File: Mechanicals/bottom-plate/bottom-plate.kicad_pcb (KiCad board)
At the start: 2 copper layers, 89 x 100 mm, 4 parts

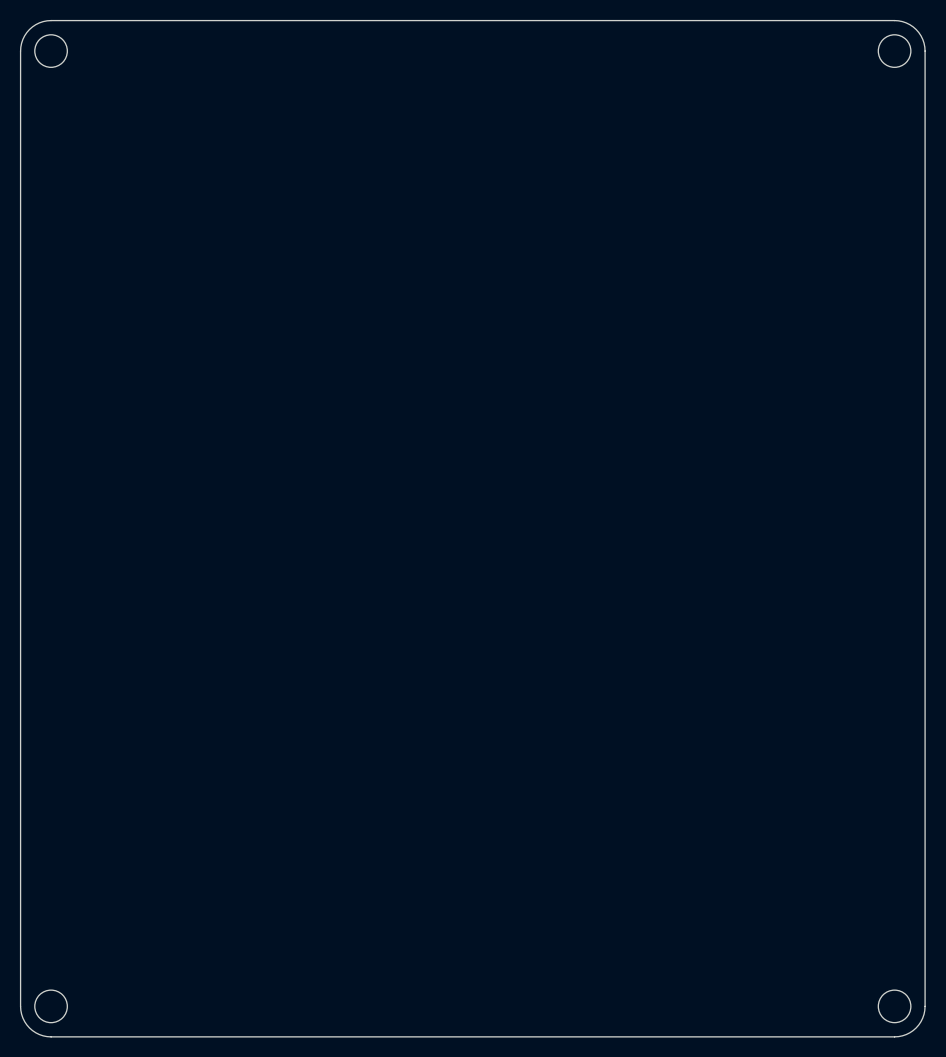
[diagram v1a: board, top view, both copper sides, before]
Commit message: move res with HS interference
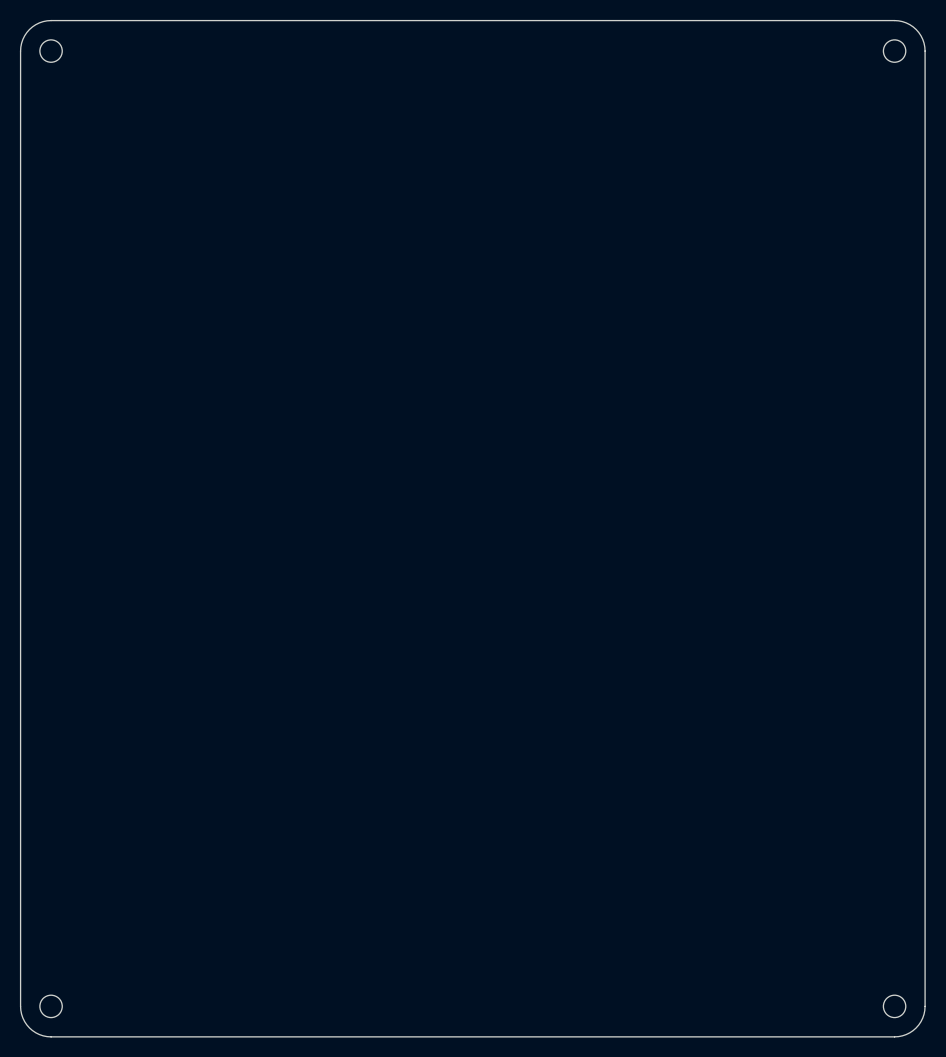
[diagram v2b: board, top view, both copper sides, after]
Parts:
- REF** (x4): value MountingHole_3.2mm_M3 -> MountingHole_2.2mm_M2; footprint MountingHole:MountingHole_3.2mm_M3 -> MountingHole:MountingHole_2.2mm_M2
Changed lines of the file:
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@@
-(kicad_pcb (version 20171130) (host pcbnew 5.1.6-c6e7f7d~87~ubuntu20.04.1)
+(kicad_pcb (version 20171130) (host pcbnew "(5.1.5)-3")
   (general
     (thickness 1.6)
@@
     (uvia_drill 0.1)
   )
-  (module MountingHole:MountingHole_3.2mm_M3 (layer F.Cu)
+  (module MountingHole:MountingHole_2.2mm_M2 (layer F.Cu)
     (at 188.15 148.55)
-    (descr "Mounting Hole 3.2mm, no annular, M3")
-    (tags "mounting hole 3.2mm no annular m3")
+    (descr "Mounting Hole 2.2mm, no annular, M2")
+    (tags "mounting hole 2.2mm no annular m2")
     (attr virtual)
     (fp_text reference REF** (at 0 -4.2) (layer F.SilkS) hide
       (effects (font (size 1 1) (thickness 0.15)))
     )
-    (fp_text value MountingHole_3.2mm_M3 (at 0 4.2) (layer F.Fab)
+    (fp_text value MountingHole_2.2mm_M2 (at 0 4.2) (layer F.Fab)
       (effects (font (size 1 1) (thickness 0.15)))
     )
-    (fp_circle (center 0 0) (end 3.45 0) (layer F.CrtYd) (width 0.05))
-    (fp_circle (center 0 0) (end 3.2 0) (layer Cmts.User) (width 0.15))
+    (fp_circle (center 0 0) (end 2.45 0) (layer F.CrtYd) (width 0.05))
+    (fp_circle (center 0 0) (end 2.2 0) (layer Cmts.User) (width 0.15))
     (fp_text user %R (at 0.3 0) (layer F.Fab) hide
       (effects (font (size 1 1) (thickness 0.15)))
     )
-    (pad 1 np_thru_hole circle (at 0 0) (size 3.2 3.2) (drill 3.2) (layers *.Cu *.Mask))
+    (pad 1 np_thru_hole circle (at 0 0) (size 2.2 2.2) (drill 2.2) (layers *.Cu *.Mask))
   )
-  (module MountingHole:MountingHole_3.2mm_M3 (layer F.Cu)
+  (module MountingHole:MountingHole_2.2mm_M2 (layer F.Cu)
     (at 105.15 148.55)
-    (descr "Mounting Hole 3.2mm, no annular, M3")
-    (tags "mounting hole 3.2mm no annular m3")
+    (descr "Mounting Hole 2.2mm, no annular, M2")
+    (tags "mounting hole 2.2mm no annular m2")
     (attr virtual)
     (fp_text reference REF** (at 0 -4.2) (layer F.SilkS) hide
       (effects (font (size 1 1) (thickness 0.15)))
     )
-    (fp_text value MountingHole_3.2mm_M3 (at 0 4.2) (layer F.Fab)
+    (fp_text value MountingHole_2.2mm_M2 (at 0 4.2) (layer F.Fab)
       (effects (font (size 1 1) (thickness 0.15)))
     )
-    (fp_circle (center 0 0) (end 3.2 0) (layer Cmts.User) (width 0.15))
-    (fp_circle (center 0 0) (end 3.45 0) (layer F.CrtYd) (width 0.05))
+    (fp_circle (center 0 0) (end 2.45 0) (layer F.CrtYd) (width 0.05))
+    (fp_circle (center 0 0) (end 2.2 0) (layer Cmts.User) (width 0.15))
     (fp_text user %R (at 0.3 0) (layer F.Fab) hide
       (effects (font (size 1 1) (thickness 0.15)))
     )
-    (pad 1 np_thru_hole circle (at 0 0) (size 3.2 3.2) (drill 3.2) (layers *.Cu *.Mask))
+    (pad 1 np_thru_hole circle (at 0 0) (size 2.2 2.2) (drill 2.2) (layers *.Cu *.Mask))
   )
-  (module MountingHole:MountingHole_3.2mm_M3 (layer F.Cu)
+  (module MountingHole:MountingHole_2.2mm_M2 (layer F.Cu)
     (at 105.15 54.55)
-    (descr "Mounting Hole 3.2mm, no annular, M3")
-    (tags "mounting hole 3.2mm no annular m3")
+    (descr "Mounting Hole 2.2mm, no annular, M2")
+    (tags "mounting hole 2.2mm no annular m2")
     (attr virtual)
     (fp_text reference REF** (at 0 -4.2) (layer F.SilkS) hide
       (effects (font (size 1 1) (thickness 0.15)))
     )
-    (fp_text value MountingHole_3.2mm_M3 (at 0 4.2) (layer F.Fab)
+    (fp_text value MountingHole_2.2mm_M2 (at 0 4.2) (layer F.Fab)
       (effects (font (size 1 1) (thickness 0.15)))
     )
-    (fp_circle (center 0 0) (end 3.45 0) (layer F.CrtYd) (width 0.05))
-    (fp_circle (center 0 0) (end 3.2 0) (layer Cmts.User) (width 0.15))
+    (fp_circle (center 0 0) (end 2.45 0) (layer F.CrtYd) (width 0.05))
+    (fp_circle (center 0 0) (end 2.2 0) (layer Cmts.User) (width 0.15))
     (fp_text user %R (at 0.3 0) (layer F.Fab) hide
       (effects (font (size 1 1) (thickness 0.15)))
     )
-    (pad 1 np_thru_hole circle (at 0 0) (size 3.2 3.2) (drill 3.2) (layers *.Cu *.Mask))
+    (pad 1 np_thru_hole circle (at 0 0) (size 2.2 2.2) (drill 2.2) (layers *.Cu *.Mask))
   )
-  (module MountingHole:MountingHole_3.2mm_M3 (layer F.Cu)
+  (module MountingHole:MountingHole_2.2mm_M2 (layer F.Cu)
     (at 188.15 54.55)
-    (descr "Mounting Hole 3.2mm, no annular, M3")
-    (tags "mounting hole 3.2mm no annular m3")
+    (descr "Mounting Hole 2.2mm, no annular, M2")
+    (tags "mounting hole 2.2mm no annular m2")
     (attr virtual)
     (fp_text reference REF** (at 0 -4.2) (layer F.SilkS) hide
       (effects (font (size 1 1) (thickness 0.15)))
     )
-    (fp_text value MountingHole_3.2mm_M3 (at 0 4.2) (layer F.Fab)
+    (fp_text value MountingHole_2.2mm_M2 (at 0 4.2) (layer F.Fab)
       (effects (font (size 1 1) (thickness 0.15)))
     )
-    (fp_circle (center 0 0) (end 3.2 0) (layer Cmts.User) (width 0.15))
-    (fp_circle (center 0 0) (end 3.45 0) (layer F.CrtYd) (width 0.05))
+    (fp_circle (center 0 0) (end 2.45 0) (layer F.CrtYd) (width 0.05))
+    (fp_circle (center 0 0) (end 2.2 0) (layer Cmts.User) (width 0.15))
     (fp_text user %R (at 0.3 0) (layer F.Fab) hide
       (effects (font (size 1 1) (thickness 0.15)))
     )
-    (pad 1 np_thru_hole circle (at 0 0) (size 3.2 3.2) (drill 3.2) (layers *.Cu *.Mask))
+    (pad 1 np_thru_hole circle (at 0 0) (size 2.2 2.2) (drill 2.2) (layers *.Cu *.Mask))
   )
   (gr_arc (start 188.15 54.55) (end 191.15 54.55) (angle -90) (layer Edge.Cuts) (width 0.05))
